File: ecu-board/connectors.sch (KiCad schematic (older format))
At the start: 19 parts, among them J10 Injector connector, J13 Chrankshaft Hall connector, J14 Camshaft Hall connector, J2 Battery power conenctor, J4 Motor conenctor, J5 Serial DB9 connector, J8 IAT connector, J9 CLT connector

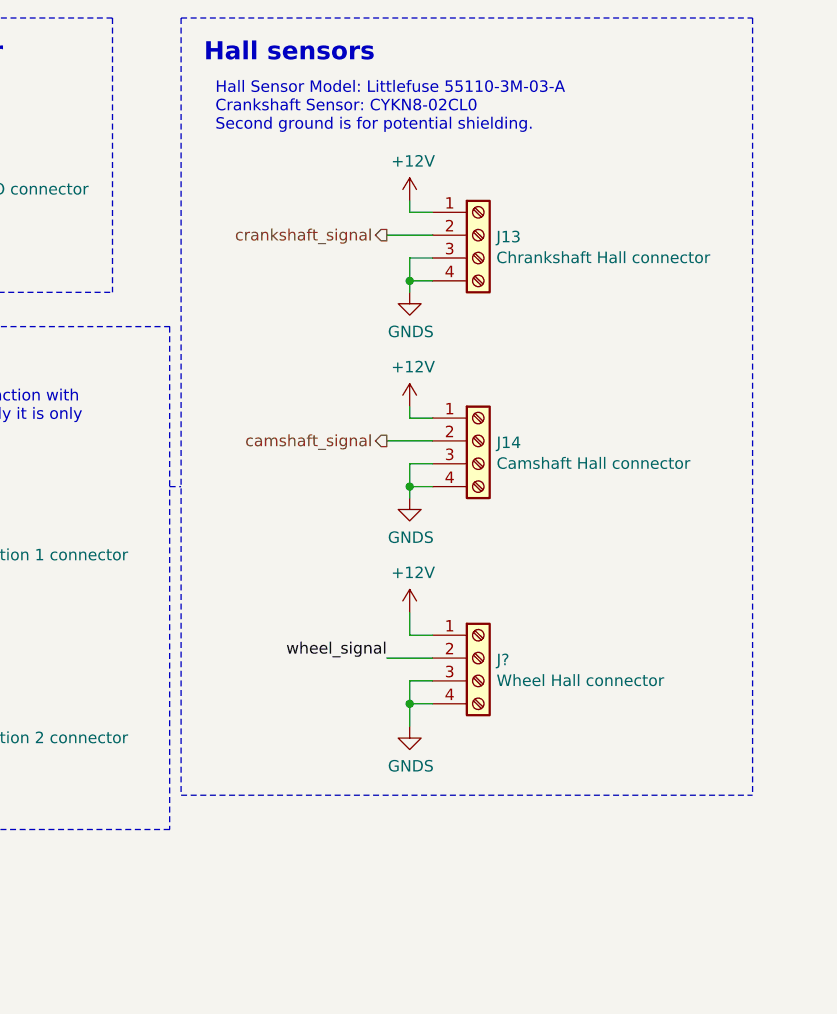
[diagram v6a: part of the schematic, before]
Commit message: Add pull up to Crankshaft hall. Resolves #16.
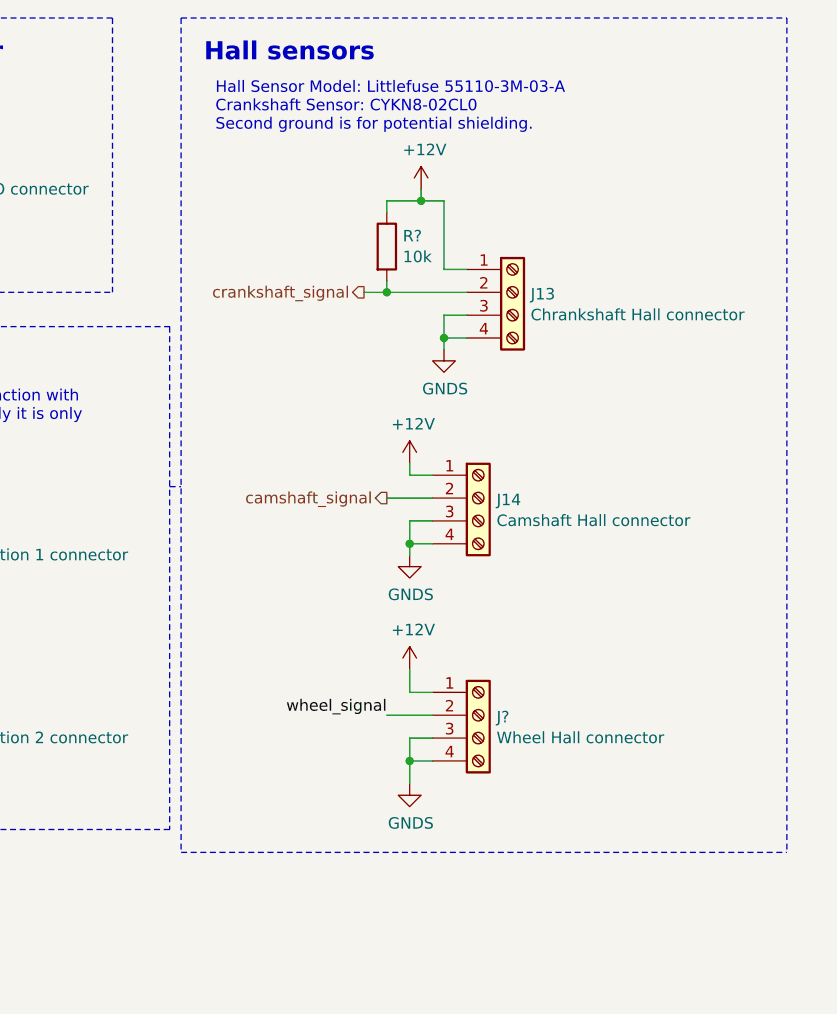
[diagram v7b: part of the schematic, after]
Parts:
- added R?: 10k, symbol Device:R
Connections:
- net +12V: now also R?.1
- net crankshaft_signal: now also R?.2
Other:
- moved on the sheet: J13, J14, J?
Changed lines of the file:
@@
 L power:+12V #PWR020
 U 1 1 5C5707AA
-P 9350 1700
-F 0 "#PWR020" H 9350 1550 50  0001 C CNN
-F 1 "+12V" H 9365 1873 50  0000 C CNN
-F 2 "" H 9350 1700 50  0001 C CNN
-F 3 "" H 9350 1700 50  0001 C CNN
-	1    9350 1700
-	1    0    0    -1
-$EndComp
-Wire Wire Line
-	9350 1700 9350 1750
-Wire Wire Line
-	9350 1750 9450 1750
+P 9400 1650
+F 0 "#PWR020" H 9400 1500 50  0001 C CNN
+F 1 "+12V" H 9415 1823 50  0000 C CNN
+F 2 "" H 9400 1650 50  0001 C CNN
+F 3 "" H 9400 1650 50  0001 C CNN
+	1    9400 1650
+	1    0    0    -1
+$EndComp
+Wire Wire Line
+	9500 2000 9600 2000
 $Comp
 L power:+12V #PWR022
 U 1 1 5C5707D6
-P 9350 2600
-F 0 "#PWR022" H 9350 2450 50  0001 C CNN
-F 1 "+12V" H 9365 2773 50  0000 C CNN
-F 2 "" H 9350 2600 50  0001 C CNN
-F 3 "" H 9350 2600 50  0001 C CNN
-	1    9350 2600
-	1    0    0    -1
-$EndComp
-Wire Wire Line
-	9350 2600 9350 2650
-Wire Wire Line
-	9350 2650 9450 2650
+P 9350 2850
+F 0 "#PWR022" H 9350 2700 50  0001 C CNN
+F 1 "+12V" H 9365 3023 50  0000 C CNN
+F 2 "" H 9350 2850 50  0001 C CNN
+F 3 "" H 9350 2850 50  0001 C CNN
+	1    9350 2850
+	1    0    0    -1
+$EndComp
+Wire Wire Line
+	9350 2850 9350 2900
+Wire Wire Line
+	9350 2900 9450 2900
 $Comp
 L power:GNDS #PWR021
 U 1 1 5C570990
-P 9350 2100
-F 0 "#PWR021" H 9350 1850 50  0001 C CNN
-F 1 "GNDS" H 9355 1927 50  0000 C CNN
-F 2 "" H 9350 2100 50  0001 C CNN
-F 3 "" H 9350 2100 50  0001 C CNN
-	1    9350 2100
-	1    0    0    -1
-$EndComp
-Wire Wire Line
-	9350 2100 9350 2050
-Wire Wire Line
-	9350 2050 9450 2050
+P 9500 2350
+F 0 "#PWR021" H 9500 2100 50  0001 C CNN
+F 1 "GNDS" H 9505 2177 50  0000 C CNN
+F 2 "" H 9500 2350 50  0001 C CNN
+F 3 "" H 9500 2350 50  0001 C CNN
+	1    9500 2350
+	1    0    0    -1
+$EndComp
+Wire Wire Line
+	9500 2350 9500 2300
+Wire Wire Line
+	9500 2300 9600 2300
 $Comp
 L power:GNDS #PWR023
 U 1 1 5C5709C2
-P 9350 3000
-F 0 "#PWR023" H 9350 2750 50  0001 C CNN
-F 1 "GNDS" H 9355 2827 50  0000 C CNN
-F 2 "" H 9350 3000 50  0001 C CNN
-F 3 "" H 9350 3000 50  0001 C CNN
-	1    9350 3000
-	1    0    0    -1
-$EndComp
-Wire Wire Line
-	9350 3000 9350 2950
-Wire Wire Line
-	9350 2950 9450 2950
-Wire Wire Line
-	9350 2950 9350 2850
-Wire Wire Line
-	9350 2850 9450 2850
-Connection ~ 9350 2950
-Wire Wire Line
-	9350 2050 9350 1950
-Wire Wire Line
-	9350 1950 9450 1950
-Connection ~ 9350 2050
+P 9350 3250
+F 0 "#PWR023" H 9350 3000 50  0001 C CNN
+F 1 "GNDS" H 9355 3077 50  0000 C CNN
+F 2 "" H 9350 3250 50  0001 C CNN
+F 3 "" H 9350 3250 50  0001 C CNN
+	1    9350 3250
+	1    0    0    -1
+$EndComp
+Wire Wire Line
+	9350 3250 9350 3200
+Wire Wire Line
+	9350 3200 9450 3200
+Wire Wire Line
+	9350 3200 9350 3100
+Wire Wire Line
+	9350 3100 9450 3100
+Connection ~ 9350 3200
+Wire Wire Line
+	9500 2300 9500 2200
+Wire Wire Line
+	9500 2200 9600 2200
+Connection ~ 9500 2300
 Text Notes 8500 1400 0    50   ~ 0
 Hall Sensor Model: Littlefuse 55110-3M-03-A\nCrankshaft Sensor: CYKN8-02CL0\nSecond ground is for potential shielding.
 Text Notes 8450 1100 0    79   ~ 16
 Hall sensors\n
-Wire Notes Line
-	8350 900  10850 900
-Wire Wire Line
-	9250 1850 9450 1850
-Wire Wire Line
-	9250 2750 9450 2750
-Text HLabel 9250 1850 0    50   Output ~ 0
+Wire Wire Line
+	9250 3000 9450 3000
+Text HLabel 9150 2100 0    50   Output ~ 0
 crankshaft_signal
-Text HLabel 9250 2750 0    50   Output ~ 0
+Text HLabel 9250 3000 0    50   Output ~ 0
 camshaft_signal
 Text Notes 6350 1100 0    79   ~ 16
@@
 L Connector:Screw_Terminal_01x04 J13
 U 1 1 5C5953F1
-P 9650 1850
-F 0 "J13" H 9729 1842 50  0000 L CNN
-F 1 "Chrankshaft Hall connector" H 9729 1751 50  0000 L CNN
-F 2 "" H 9650 1850 50  0001 C CNN
-F 3 "~" H 9650 1850 50  0001 C CNN
-F 4 "2315043, 2315064" H 9650 1850 50  0001 C CNN "Farnell"
-	1    9650 1850
+P 9800 2100
+F 0 "J13" H 9879 2092 50  0000 L CNN
+F 1 "Chrankshaft Hall connector" H 9879 2001 50  0000 L CNN
+F 2 "" H 9800 2100 50  0001 C CNN
+F 3 "~" H 9800 2100 50  0001 C CNN
+F 4 "2315043, 2315064" H 9800 2100 50  0001 C CNN "Farnell"
+	1    9800 2100
 	1    0    0    -1
 $EndComp
@@
 L Connector:Screw_Terminal_01x04 J14
 U 1 1 5C596299
-P 9650 2750
-F 0 "J14" H 9730 2742 50  0000 L CNN
-F 1 "Camshaft Hall connector" H 9730 2651 50  0000 L CNN
-F 2 "" H 9650 2750 50  0001 C CNN
-F 3 "~" H 9650 2750 50  0001 C CNN
-F 4 "2315043, 2315064" H 9650 2750 50  0001 C CNN "Farnell"
-	1    9650 2750
+P 9650 3000
+F 0 "J14" H 9730 2992 50  0000 L CNN
+F 1 "Camshaft Hall connector" H 9730 2901 50  0000 L CNN
+F 2 "" H 9650 3000 50  0001 C CNN
+F 3 "~" H 9650 3000 50  0001 C CNN
+F 4 "2315043, 2315064" H 9650 3000 50  0001 C CNN "Farnell"
+	1    9650 3000
 	1    0    0    -1
 $EndComp
@@
 L Connector:Screw_Terminal_01x04 J?
 U 1 1 5C788398
-P 9650 3700
-F 0 "J?" H 9730 3692 50  0000 L CNN
-F 1 "Wheel Hall connector" H 9730 3601 50  0000 L CNN
-F 2 "" H 9650 3700 50  0001 C CNN
-F 3 "~" H 9650 3700 50  0001 C CNN
-F 4 "2315043, 2315064" H 9650 3700 50  0001 C CNN "Farnell"
-	1    9650 3700
+P 9650 3950
+F 0 "J?" H 9730 3942 50  0000 L CNN
+F 1 "Wheel Hall connector" H 9730 3851 50  0000 L CNN
+F 2 "" H 9650 3950 50  0001 C CNN
+F 3 "~" H 9650 3950 50  0001 C CNN
+F 4 "2315043, 2315064" H 9650 3950 50  0001 C CNN "Farnell"
+	1    9650 3950
 	1    0    0    -1
 $EndComp
@@
 L power:+12V #PWR?
 U 1 1 5C7883EF
-P 9350 3500
-F 0 "#PWR?" H 9350 3350 50  0001 C CNN
-F 1 "+12V" H 9365 3673 50  0000 C CNN
-F 2 "" H 9350 3500 50  0001 C CNN
-F 3 "" H 9350 3500 50  0001 C CNN
-	1    9350 3500
+P 9350 3750
+F 0 "#PWR?" H 9350 3600 50  0001 C CNN
+F 1 "+12V" H 9365 3923 50  0000 C CNN
+F 2 "" H 9350 3750 50  0001 C CNN
+F 3 "" H 9350 3750 50  0001 C CNN
+	1    9350 3750
 	1    0    0    -1
 $EndComp
@@
 L power:GNDS #PWR?
 U 1 1 5C78841E
-P 9350 4000
-F 0 "#PWR?" H 9350 3750 50  0001 C CNN
-F 1 "GNDS" H 9355 3827 50  0000 C CNN
-F 2 "" H 9350 4000 50  0001 C CNN
-F 3 "" H 9350 4000 50  0001 C CNN
-	1    9350 4000
-	1    0    0    -1
-$EndComp
-Text Label 9250 3700 2    50   ~ 0
+P 9350 4250
+F 0 "#PWR?" H 9350 4000 50  0001 C CNN
+F 1 "GNDS" H 9355 4077 50  0000 C CNN
+F 2 "" H 9350 4250 50  0001 C CNN
+F 3 "" H 9350 4250 50  0001 C CNN
+	1    9350 4250
+	1    0    0    -1
+$EndComp
+Text Label 9250 3950 2    50   ~ 0
 wheel_signal
 Wire Wire Line
-	9250 3700 9450 3700
-Wire Wire Line
-	9450 3600 9350 3600
-Wire Wire Line
-	9350 3600 9350 3500
-Wire Wire Line
-	9450 3800 9350 3800
-Wire Wire Line
-	9350 3800 9350 3900
-Wire Wire Line
-	9450 3900 9350 3900
-Connection ~ 9350 3900
-Wire Wire Line
-	9350 3900 9350 4000
+	9250 3950 9450 3950
+Wire Wire Line
+	9450 3850 9350 3850
+Wire Wire Line
+	9350 3850 9350 3750
+Wire Wire Line
+	9450 4050 9350 4050
+Wire Wire Line
+	9350 4050 9350 4150
+Wire Wire Line
+	9450 4150 9350 4150
+Connection ~ 9350 4150
+Wire Wire Line
+	9350 4150 9350 4250
 Text Label 4700 6050 2    50   ~ 0
 wheel_signal
-Wire Notes Line
-	8350 4300 10850 4300
-Wire Notes Line
-	10850 900  10850 4300
-Wire Notes Line
-	8350 900  8350 4300
 Text HLabel 4700 6250 0    50   BiDi ~ 0
 serial_rx
@@
 Wire Notes Line
 	3700 7100 3700 4900
+$Comp
+L Device:R R?
+U 1 1 5C9BB785
+P 9250 1900
+F 0 "R?" H 9320 1946 50  0000 L CNN
+F 1 "10k" H 9320 1855 50  0000 L CNN
+F 2 "" V 9180 1900 50  0001 C CNN
+F 3 "~" H 9250 1900 50  0001 C CNN
+	1    9250 1900
+	1    0    0    -1
+$EndComp
+Wire Wire Line
+	9150 2100 9250 2100
+Wire Wire Line
+	9250 2050 9250 2100
+Connection ~ 9250 2100
+Wire Wire Line
+	9250 2100 9600 2100
+Wire Wire Line
+	9250 1750 9250 1700
+Wire Wire Line
+	9250 1700 9400 1700
+Wire Wire Line
+	9400 1700 9400 1650
+Wire Wire Line
+	9400 1700 9500 1700
+Wire Wire Line
+	9500 1700 9500 2000
+Connection ~ 9400 1700
+Wire Notes Line
+	8350 900  11000 900
+Wire Notes Line
+	8350 900  8350 4550
+Wire Notes Line
+	8350 4550 11000 4550
+Wire Notes Line
+	11000 900  11000 4550
 $EndSCHEMATC

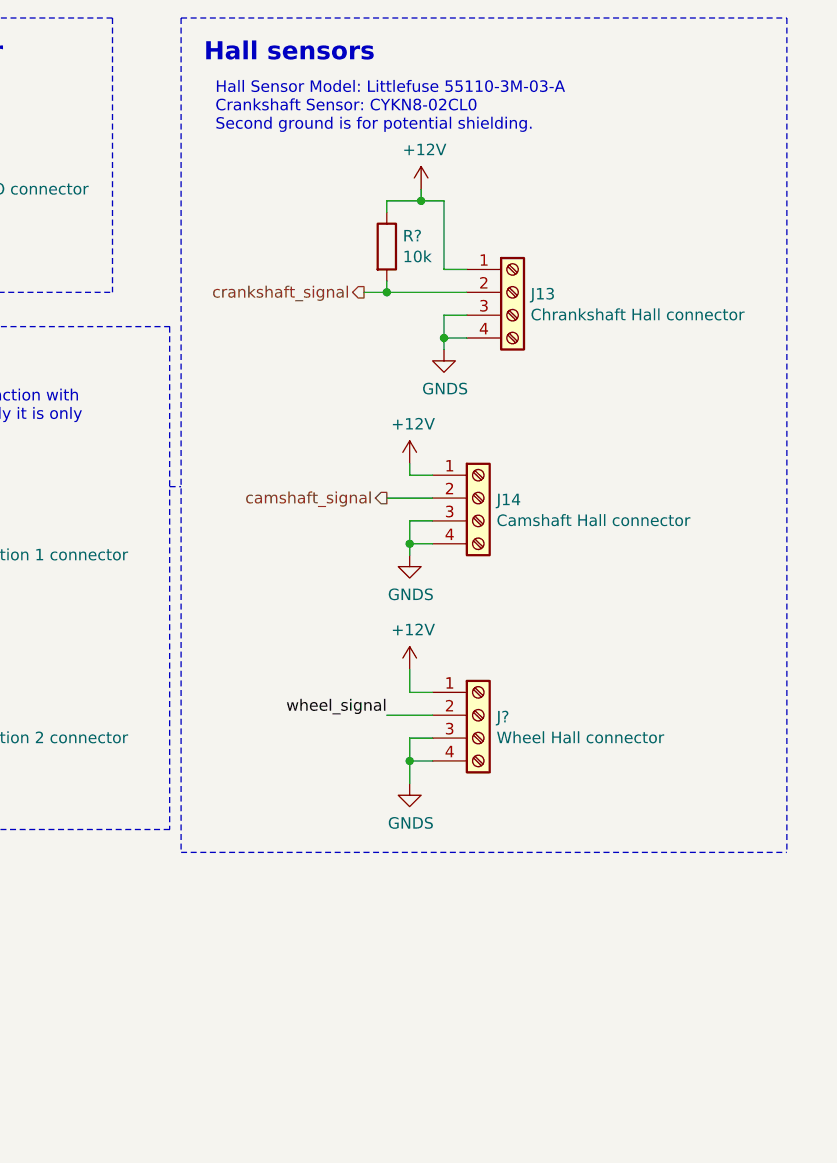
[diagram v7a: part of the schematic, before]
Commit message: Add pull up placeholders to hall sensors. Resolves #18
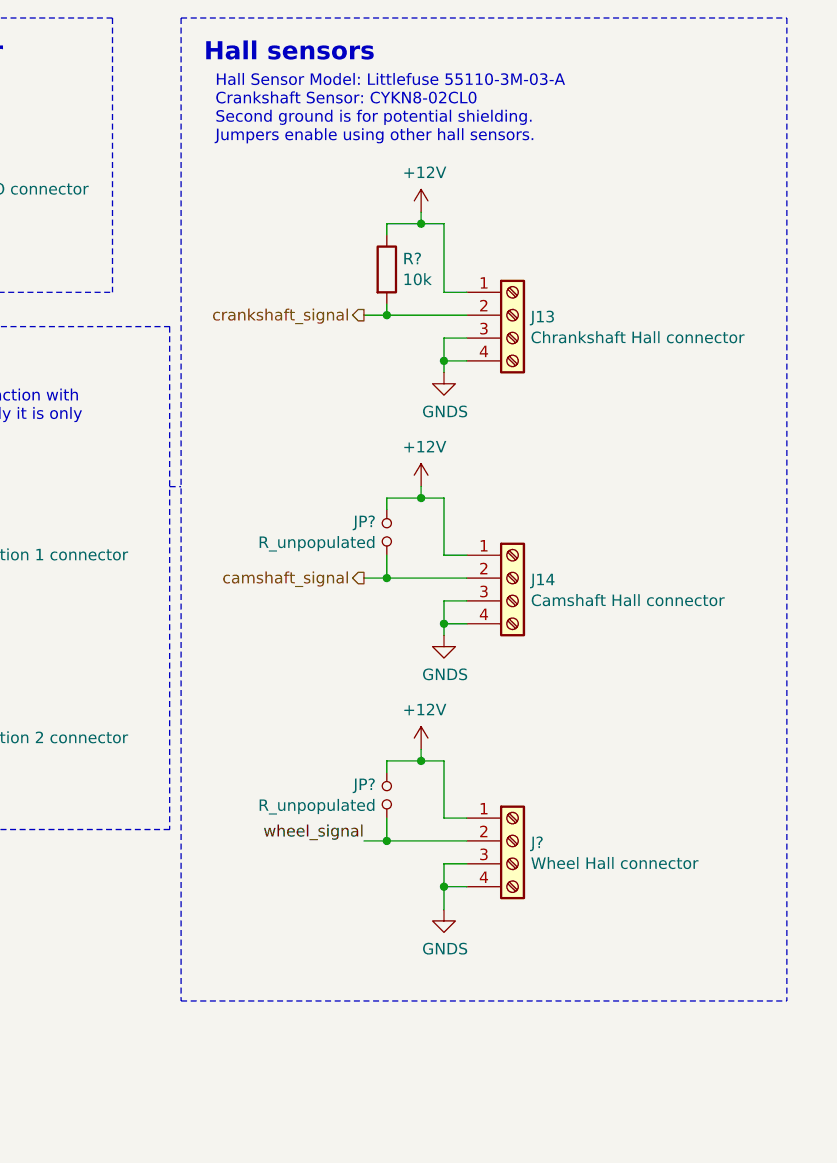
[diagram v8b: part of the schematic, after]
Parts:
- added JP? (x2): R_unpopulated, symbol Device:Jumper_NO_Small
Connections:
- net +12V: now also JP?.2, JP?.2
- net camshaft_signal: now also JP?.1
- net wheel_signal: now also JP?.1
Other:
- note added: "Hall Sensor Model: Littlefuse 55110-3M-03-A\nCrankshaft Sensor: CYKN8-02CL0\nSecond ground is for potential shielding.\nJumpers enable using other hall sensors."
- note removed: "Hall Sensor Model: Littlefuse 55110-3M-03-A\nCrankshaft Sensor: CYKN8-02CL0\nSecond ground is for potential shielding."
- moved on the sheet: J13, J14, J?, R?
